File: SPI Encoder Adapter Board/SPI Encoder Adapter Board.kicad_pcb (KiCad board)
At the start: 2 copper layers, 15.2 x 28 mm, 4 parts, among them J1 Conn_01x08, J2 Conn_01x08

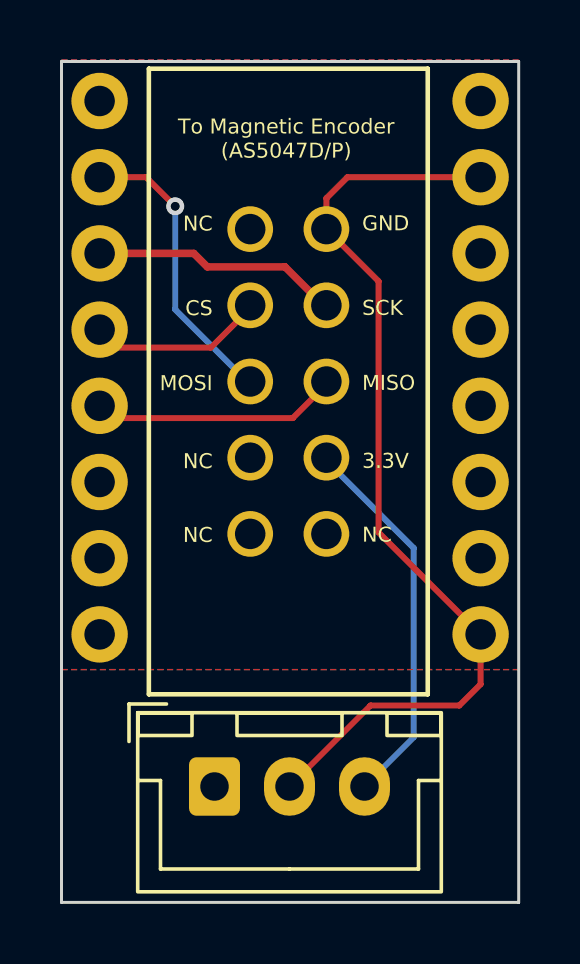
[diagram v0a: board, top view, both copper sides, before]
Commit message: removed port outlines on PCBs
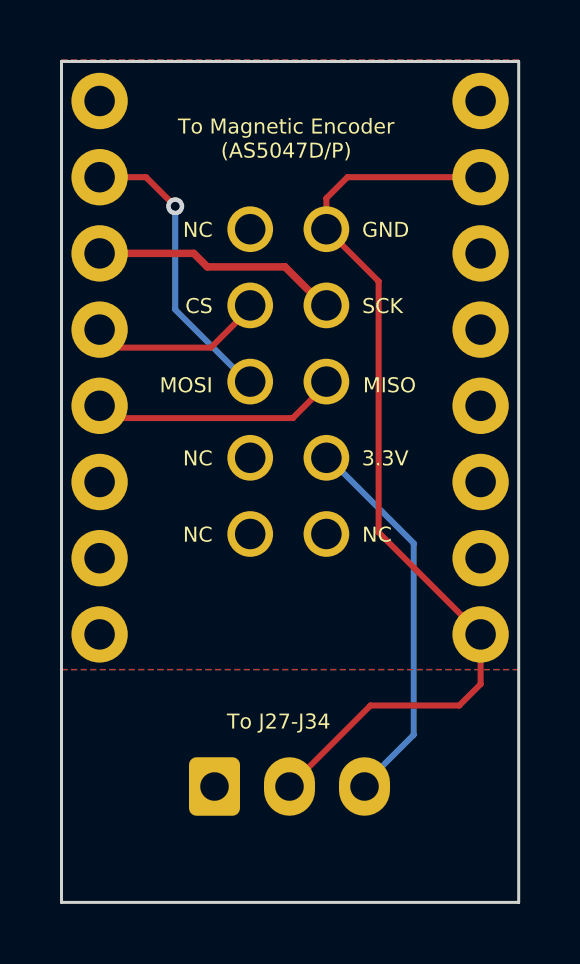
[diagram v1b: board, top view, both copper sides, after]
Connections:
- J2 pad 7: 3.3V -> (no net)
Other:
- board text added: "Designed by Kevin Guo for Sarah Meyohas Studio in 2026"
- board text added: "To J27-J34"
